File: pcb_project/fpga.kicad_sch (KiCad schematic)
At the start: 53 parts, among them J7 FTSH-107-01-F-DV-K, Q1 BC847BPN, Q2 BC857BS, SW3 SW_Push, U1 XC7A100T-FTG256

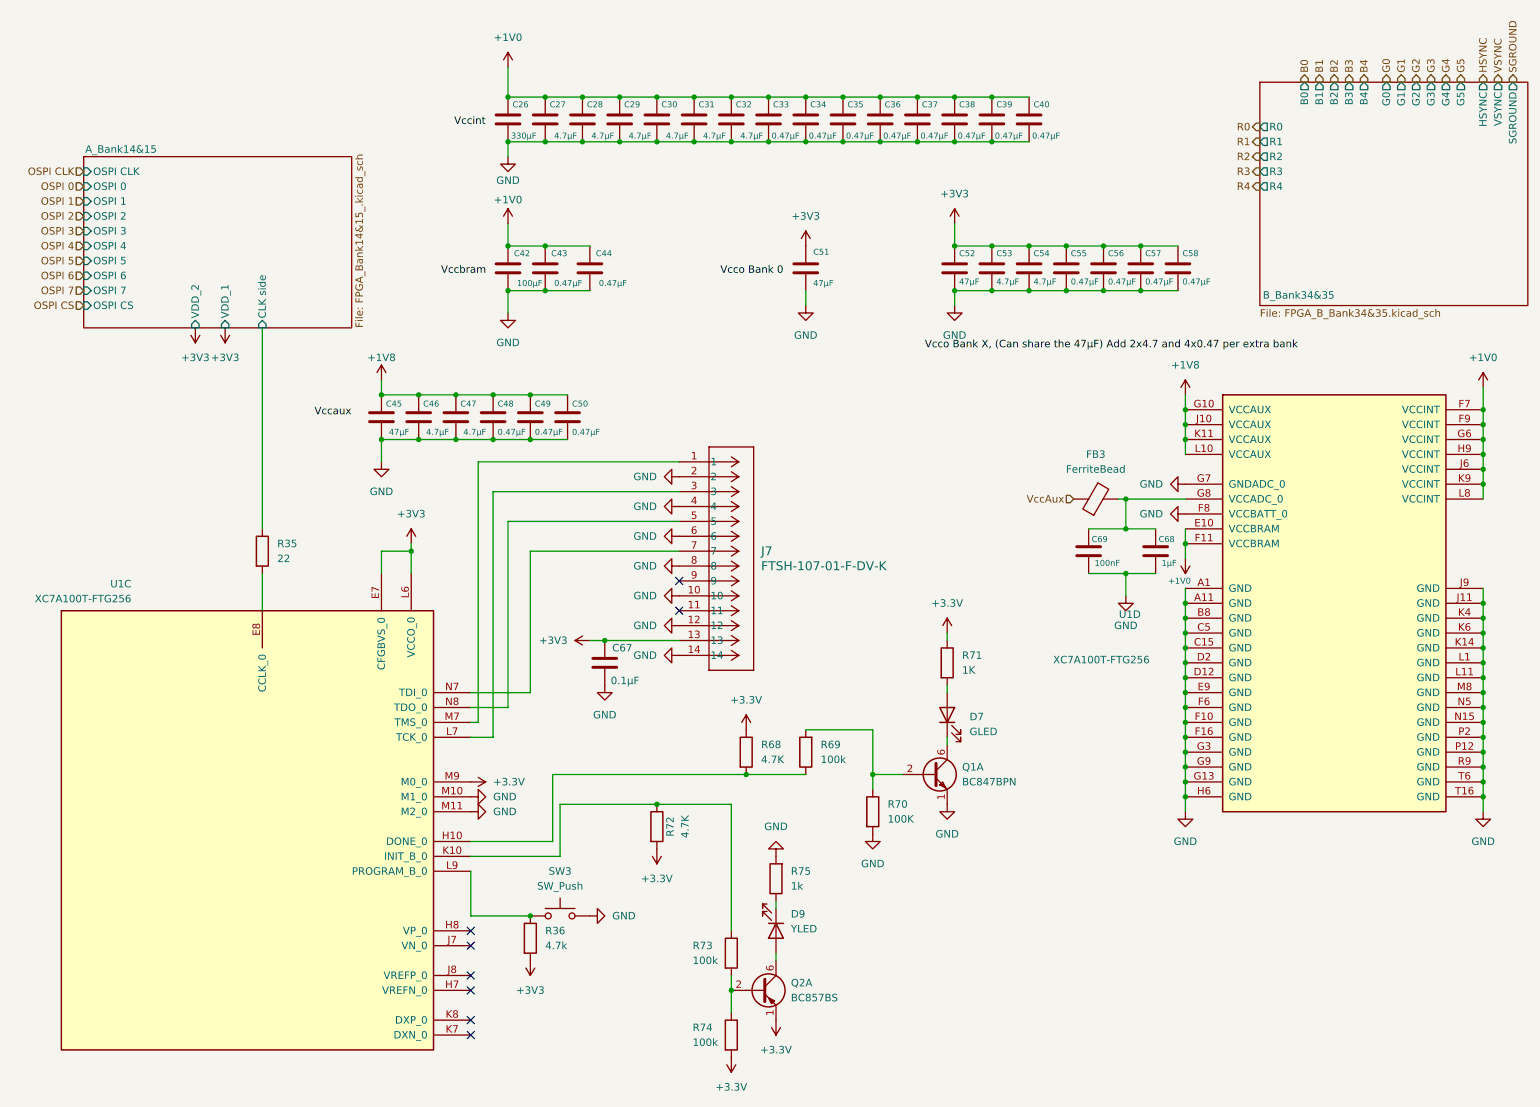
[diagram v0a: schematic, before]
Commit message: ERC fixes, some remain
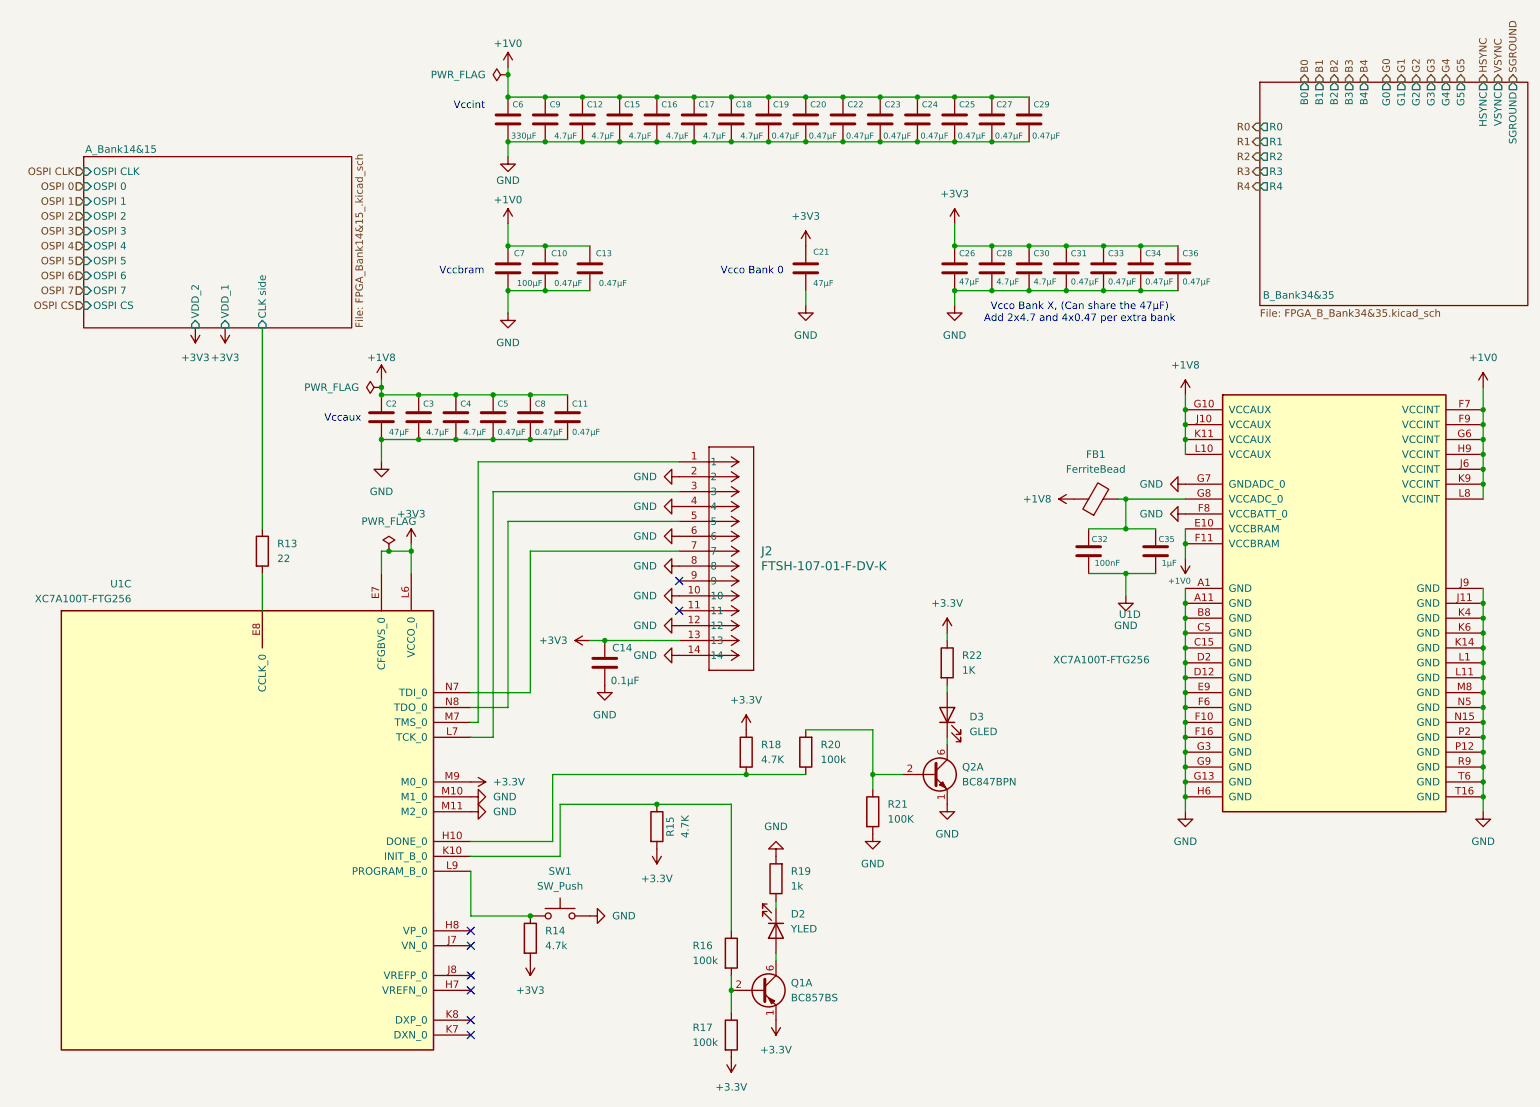
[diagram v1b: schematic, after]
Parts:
- renumbered C43 to C10, C50 to C11, C28 to C12, C44 to C13, C67 to C14, C29 to C15, C30 to C16, C31 to C17, C32 to C18, C33 to C19, C45 to C2, C34 to C20, C51 to C21, C35 to C22, C36 to C23, C37 to C24, C38 to C25, C52 to C26, C39 to C27, C53 to C28, C40 to C29, C46 to C3, C54 to C30, C55 to C31, C69 to C32, C56 to C33, C57 to C34, C68 to C35, C58 to C36, C47 to C4, C48 to C5, C26 to C6, C42 to C7, C49 to C8, C27 to C9, D9 to D2, D7 to D3, FB3 to FB1, J7 to J2, Q2 to Q1, Q1 to Q2, R35 to R13, R36 to R14, R72 to R15, R73 to R16, R74 to R17, R68 to R18, R75 to R19, R69 to R20, R70 to R21, R71 to R22, SW3 to SW1
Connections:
- net VccAux is gone; now on net +1V8: FB1.1
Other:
- note added: "Vccaux"
- note added: "Vccbram"
- note added: "Vccint"
- note added: "Vcco Bank 0"
- note added: "Vcco Bank X, (Can share the 47µF) Add 2x4.7 and 4x0.47 per extra bank"

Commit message: ERC done
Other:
- sheet A_Bank14&15 ports: added none; removed VDD_1, VDD_2
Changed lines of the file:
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@@
 	)
 	(symbol
-		(lib_id "power:+3V3")
-		(at 48.26 64.77 180)
-		(unit 1)
-		(exclude_from_sim no)
-		(in_bom yes)
-		(on_board yes)
-		(dnp no)
-		(fields_autoplaced yes)
-		(property "Reference" "#PWR04"
-			(at 48.26 60.96 0)
-			(effects
-				(font
-					(size 1.27 1.27)
-				)
-				(hide yes)
-			)
-		)
-		(property "Value" "+3V3"
-			(at 48.26 69.85 0)
-			(effects
-				(font
-					(size 1.27 1.27)
-				)
-			)
-		)
-		(property "Footprint" ""
-			(at 48.26 64.77 0)
-			(effects
-				(font
-					(size 1.27 1.27)
-				)
-				(hide yes)
-			)
-		)
-		(property "Datasheet" ""
-			(at 48.26 64.77 0)
-			(effects
-				(font
-					(size 1.27 1.27)
-				)
-				(hide yes)
-			)
-		)
-		(property "Description" "Power symbol creates a global label with name \"+3V3\""
-			(at 48.26 64.77 0)
-			(effects
-				(font
-					(size 1.27 1.27)
-				)
-				(hide yes)
-			)
-		)
-		(pin "1"
-		)
-		(instances
-			(project ""
-				(path "/98f80f66-4595-4d0f-90ca-59b2db6f447b/8bdc4eb6-105b-4ccb-b86f-5b5221dfef47"
-					(reference "#PWR04")
-					(unit 1)
-				)
-			)
-		)
-	)
-	(symbol
 		(lib_id "Device:LED")
 		(at 147.32 167.64 270)
@@
 	)
 	(symbol
-		(lib_id "power:+3V3")
-		(at 53.34 64.77 180)
-		(unit 1)
-		(exclude_from_sim no)
-		(in_bom yes)
-		(on_board yes)
-		(dnp no)
-		(fields_autoplaced yes)
-		(property "Reference" "#PWR05"
-			(at 53.34 60.96 0)
-			(effects
-				(font
-					(size 1.27 1.27)
-				)
-				(hide yes)
-			)
-		)
-		(property "Value" "+3V3"
-			(at 53.34 69.85 0)
-			(effects
-				(font
-					(size 1.27 1.27)
-				)
-			)
-		)
-		(property "Footprint" ""
-			(at 53.34 64.77 0)
-			(effects
-				(font
-					(size 1.27 1.27)
-				)
-				(hide yes)
-			)
-		)
-		(property "Datasheet" ""
-			(at 53.34 64.77 0)
-			(effects
-				(font
-					(size 1.27 1.27)
-				)
-				(hide yes)
-			)
-		)
-		(property "Description" "Power symbol creates a global label with name \"+3V3\""
-			(at 53.34 64.77 0)
-			(effects
-				(font
-					(size 1.27 1.27)
-				)
-				(hide yes)
-			)
-		)
-		(pin "1"
-		)
-		(instances
-			(project ""
-				(path "/98f80f66-4595-4d0f-90ca-59b2db6f447b/8bdc4eb6-105b-4ccb-b86f-5b5221dfef47"
-					(reference "#PWR05")
-					(unit 1)
-				)
-			)
-		)
-	)
-	(symbol
 		(lib_id "Device:C")
 		(at 215.9 54.61 0)
@@
 			(effects
 				(font
-					(size 1.27 1.27)
-				)
-				(justify left)
-			)
-		)
-		(pin "VDD_2" input
-			(at 48.26 64.77 270)
-			(effects
-				(font
-					(size 1.27 1.27)
-				)
-				(justify left)
-			)
-		)
-		(pin "VDD_1" input
-			(at 53.34 64.77 270)
-			(effects
-				(font

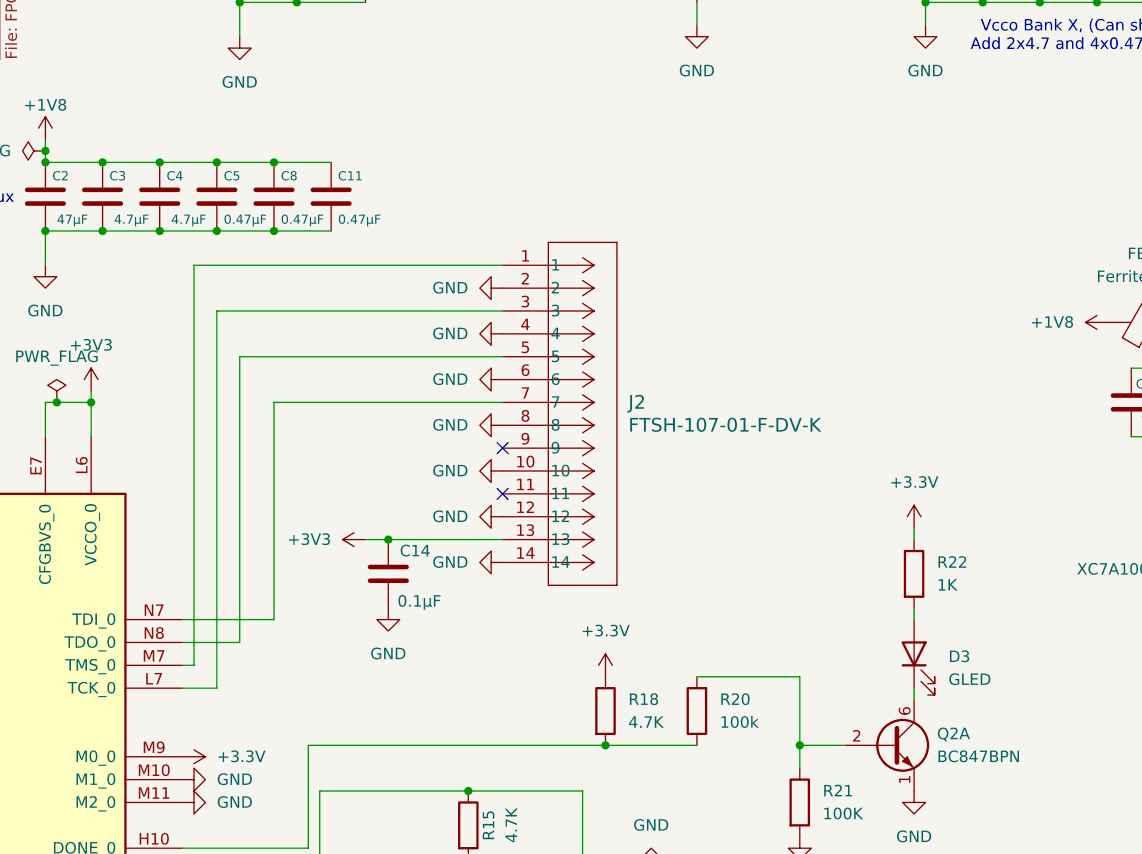
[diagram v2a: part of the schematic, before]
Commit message: Fix JTAG connector, add pullups (FPGA has internal pullups as well), add some capacitor footprints
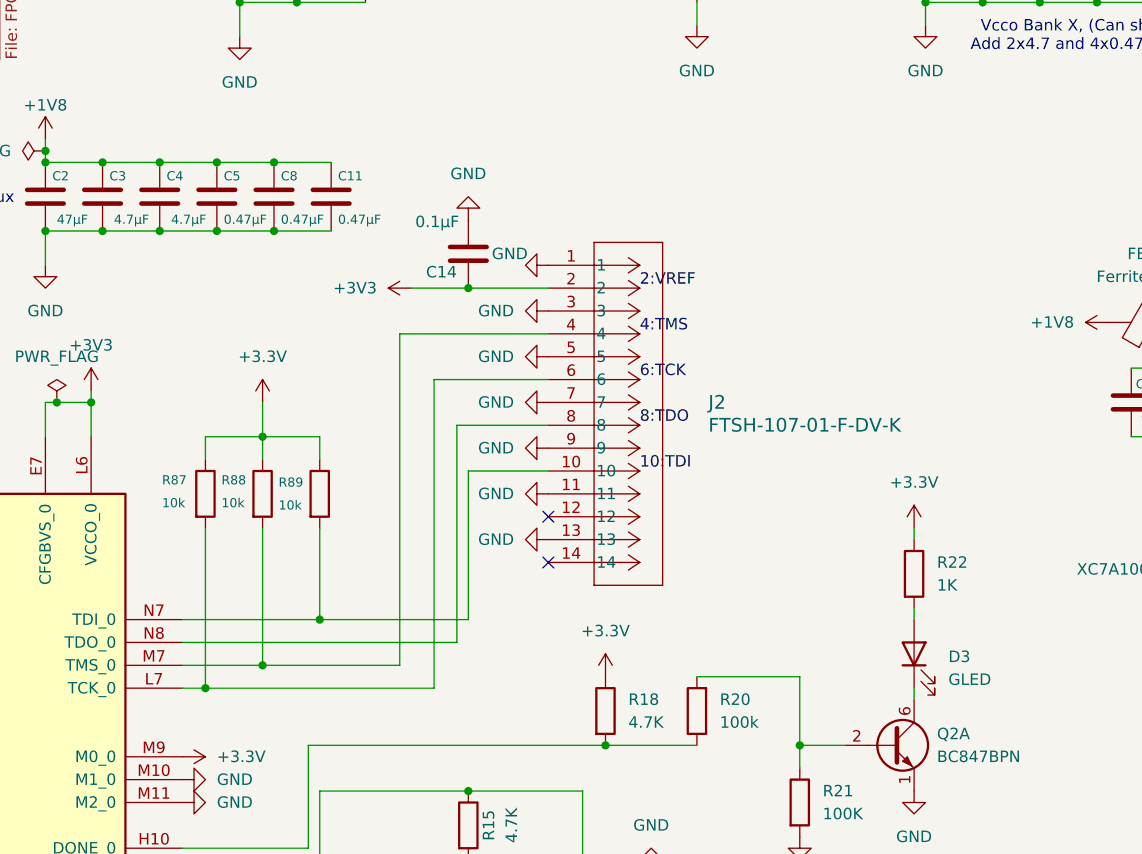
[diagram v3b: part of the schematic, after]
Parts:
- added R87, R88, R89: 10k, symbol Device:R
- C10, C11, C12, C13, C15, C16, C17, C18, C19, C20, C22, C23, C24, C25, C27, C28, C29, C3, C30, C31, C33, C34, C36, C4, C5, C8, C9: footprint (none) -> Capacitor_SMD:C_0805_2012Metric_Pad1.18x1.45mm_HandSolder
- C2, C21, C26: footprint (none) -> Capacitor_SMD:C_1210_3225Metric_Pad1.33x2.70mm_HandSolder
- C32: footprint (none) -> Capacitor_SMD:C_0603_1608Metric_Pad1.08x0.95mm_HandSolder
- C6: footprint (none) -> Capacitor_SMD:CP_Elec_10x10.5
- J2: footprint CON14_2X7_DUK_FTSH_SAI -> Project_Footprints:CON14_2X7_DUK_FTSH_SAI
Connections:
- net +3.3V: now also R87.1, R88.1, R89.1
- net +3V3: now also J2.2; no longer J2.13
- net GND: now also J2.1, J2.11, J2.13, J2.3, J2.5, J2.7, J2.9; no longer J2.10, J2.12, J2.14, J2.2, J2.4, J2.6, J2.8
- net at U1.M7 (TMS_0): now also J2.4, R88.2; no longer J2.1
- net at U1.L7 (TCK_0): now also J2.6, R87.2; no longer J2.3
- net at U1.N8 (TDO_0): now also J2.8; no longer J2.5
- net at U1.N7 (TDI_0): now also J2.10, R89.2; no longer J2.7
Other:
- moved on the sheet: C14, J2

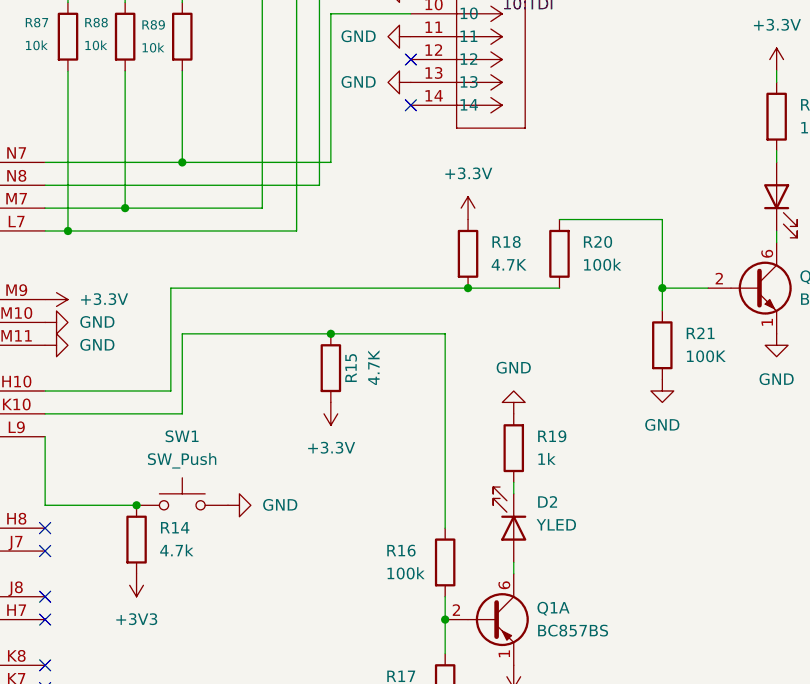
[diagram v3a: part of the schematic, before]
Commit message: Add FPGA DONE AND PROGRAM_B (reset) to MCU GPIO
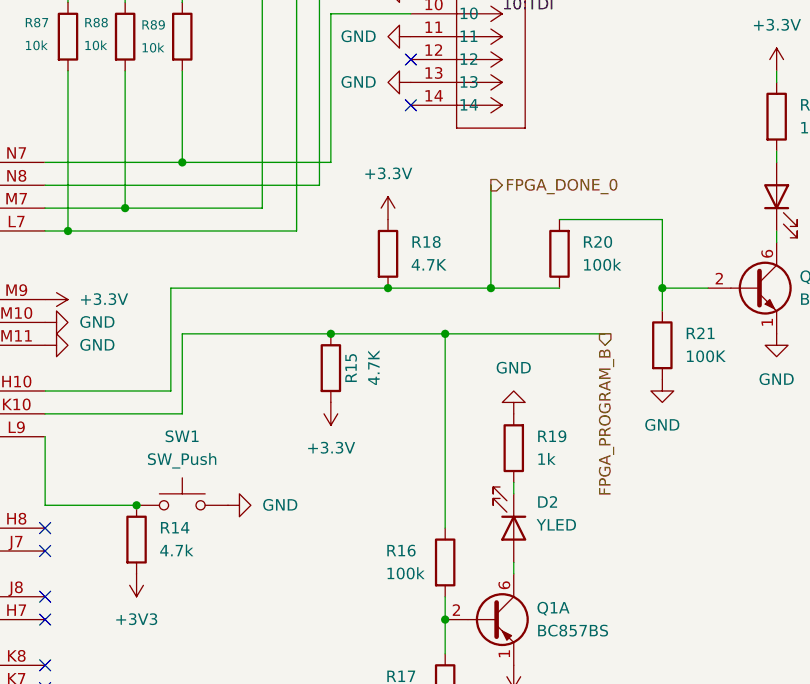
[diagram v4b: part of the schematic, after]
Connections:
- net FPGA_DONE_0: now reaches R18.2, R20.1, U1.H10 (DONE_0)
- net FPGA_PROGRAM_B: now reaches R15.1, R16.1, U1.K10 (INIT_B_0)
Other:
- moved on the sheet: R18
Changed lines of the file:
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@@
 	)
 	(junction
+		(at 133.35 140.97)
+		(diameter 0)
+		(color 0 0 0 0)
+	)
+	(junction
 		(at 267.97 91.44)
 		(diameter 0)
@@
 	)
 	(junction
+		(at 144.78 140.97)
+		(diameter 0)
+		(color 0 0 0 0)
+	)
+	(junction
 		(at 217.17 111.76)
 		(diameter 0)
@@
 	)
 	(junction
-		(at 142.24 140.97)
-		(diameter 0)
-		(color 0 0 0 0)
-	)
-	(junction
 		(at 190.5 58.42)
 		(diameter 0)
@@
 		(color 0 0 0 0)
 	)
+	(junction
+		(at 139.7 146.05)
+		(diameter 0)
+		(color 0 0 0 0)
+	)
 	(no_connect
 		(at 95.25 167.64)
@@
 	(wire
 		(pts
-			(xy 109.22 140.97) (xy 142.24 140.97)
+			(xy 109.22 140.97) (xy 133.35 140.97)
 		)
 		(stroke
@@
 	(wire
 		(pts
+			(xy 139.7 146.05) (xy 157.48 146.05)
+		)
+		(stroke
+			(width 0)
+			(type default)
+		)
+	)
+	(wire
+		(pts
 			(xy 125.73 105.41) (xy 125.73 129.54)
 		)
@@
 	(wire
 		(pts
+			(xy 144.78 129.54) (xy 144.78 140.97)
+		)
+		(stroke
+			(width 0)
+			(type default)
+		)
+	)
+	(wire
+		(pts
 			(xy 217.17 114.3) (xy 217.17 116.84)
 		)
@@
 	(wire
 		(pts
-			(xy 142.24 140.97) (xy 152.4 140.97)
-		)
-		(stroke
-			(width 0)
-			(type default)
-		)
-	)
-	(wire
-		(pts
 			(xy 177.8 46.99) (xy 177.8 50.8)
 		)
@@
 	(wire
 		(pts
+			(xy 144.78 140.97) (xy 152.4 140.97)
+		)
+		(stroke
+			(width 0)
+			(type default)
+		)
+	)
+	(wire
+		(pts
 			(xy 267.97 137.16) (xy 267.97 139.7)
 		)
@@
 	(wire
 		(pts
+			(xy 133.35 140.97) (xy 144.78 140.97)
+		)
+		(stroke
+			(width 0)
+			(type default)
+		)
+	)
+	(wire
+		(pts
 			(xy 184.15 25.4) (xy 190.5 25.4)
 		)
@@
 		)
 	)
+	(hierarchical_label "FPGA_DONE_0"
+		(shape output)
+		(at 144.78 129.54 0)
+		(effects
+			(font
+				(size 1.27 1.27)
+			)
+			(justify left)
+		)
+	)
 	(hierarchical_label "OSPI CLK"
 		(shape input)
@@
 		)
 	)
+	(hierarchical_label "FPGA_PROGRAM_B"
+		(shape output)
+		(at 157.48 146.05 270)
+		(effects
+			(font
+				(size 1.27 1.27)
+			)
+			(justify right)
+		)
+	)
 	(hierarchical_label "SGROUND"
 		(shape output)
@@
 	(symbol
 		(lib_id "Device:R")
-		(at 142.24 137.16 0)
+		(at 133.35 137.16 0)
 		(unit 1)
 		(exclude_from_sim no)
@@
 		(fields_autoplaced yes)
 		(property "Reference" "R18"
-			(at 144.78 135.8899 0)
+			(at 135.89 135.8899 0)
 			(effects
 				(font
@@
 		)
 		(property "Value" "4.7K"
-			(at 144.78 138.4299 0)
+			(at 135.89 138.4299 0)
 			(effects
 				(font
@@
 		)
 		(property "Footprint" ""
-			(at 140.462 137.16 90)
+			(at 131.572 137.16 90)
 			(effects
 				(font
@@
 		)
 		(property "Datasheet" "~"
-			(at 142.24 137.16 0)
+			(at 133.35 137.16 0)
 			(effects
 				(font
@@
 		)
 		(property "Description" "Resistor"
-			(at 142.24 137.16 0)
+			(at 133.35 137.16 0)
 			(effects
 				(font
@@
 	(symbol
 		(lib_id "power:+3.3V")
-		(at 142.24 133.35 0)
+		(at 133.35 133.35 0)
 		(unit 1)
 		(exclude_from_sim no)
@@
 		(fields_autoplaced yes)
 		(property "Reference" "#PWR029"
-			(at 142.24 137.16 0)
+			(at 133.35 137.16 0)
 			(effects
 				(font
@@
 		)
 		(property "Value" "+3.3V"
-			(at 142.24 128.27 0)
+			(at 133.35 128.27 0)
 			(effects
 				(font
@@
 		)
 		(property "Footprint" ""
-			(at 142.24 133.35 0)
+			(at 133.35 133.35 0)
 			(effects
 				(font
@@
 		)
 		(property "Datasheet" ""
-			(at 142.24 133.35 0)
+			(at 133.35 133.35 0)
 			(effects
 				(font
@@
 		)
 		(property "Description" "Power symbol creates a global label with name \"+3.3V\""
-			(at 142.24 133.35 0)
+			(at 133.35 133.35 0)
 			(effects
 				(font
